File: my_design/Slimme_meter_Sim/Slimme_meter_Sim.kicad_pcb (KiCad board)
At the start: 2 copper layers, 29 parts, among them CN1 S2B-PH-SM4-TB, SW1 MSK12C02, U1 USBLC6-2SC6-ES, U2 BQ25185DLHR, U3 TPS61023DRLR

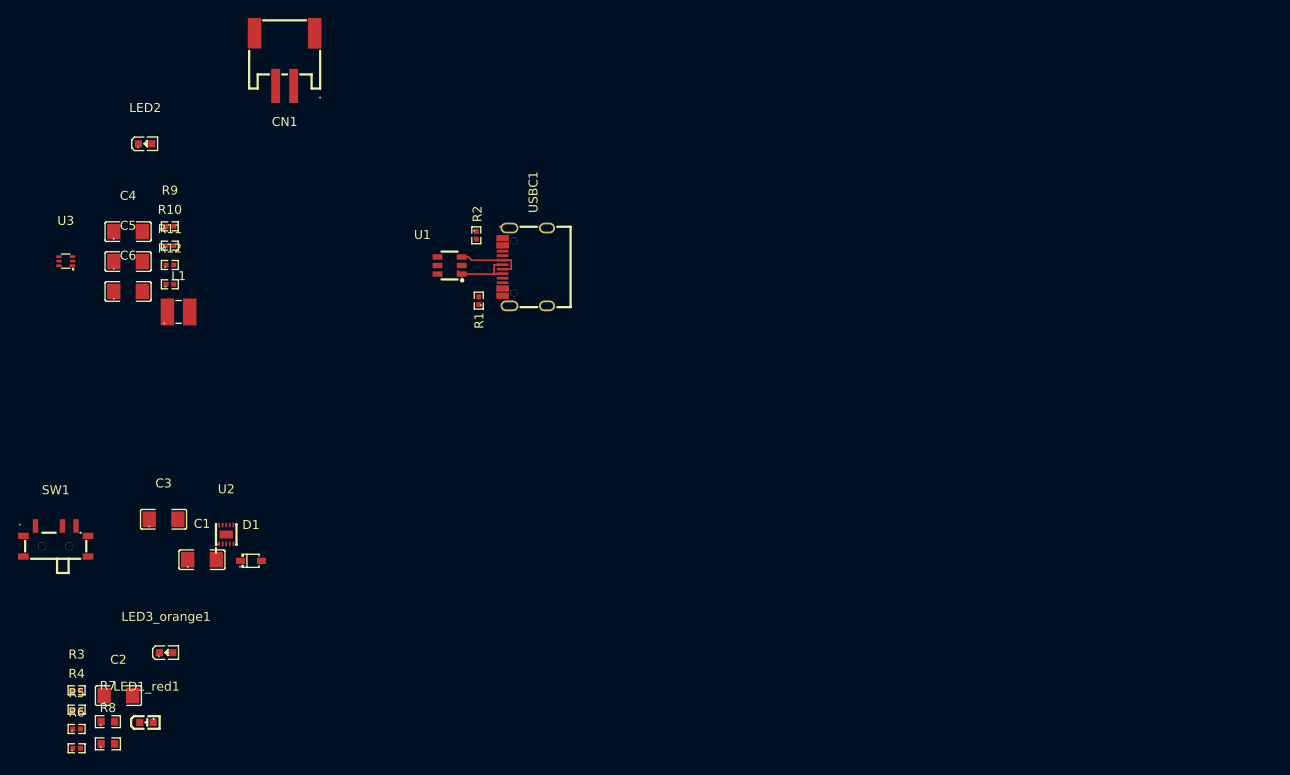
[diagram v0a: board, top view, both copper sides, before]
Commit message: Add sheet-2 power/MCU schematic progress and document P1 opto domains.
Captures TPS26625, SY8088 3V3, ESP32-C3, RJ12 placement, and README guidance that Request/Data optos keep UART on 3.3 V while pin 5 stays open-collector on the 5 V P1 side.

Co-authored-by: Cursor <cursoragent@cursor.com>
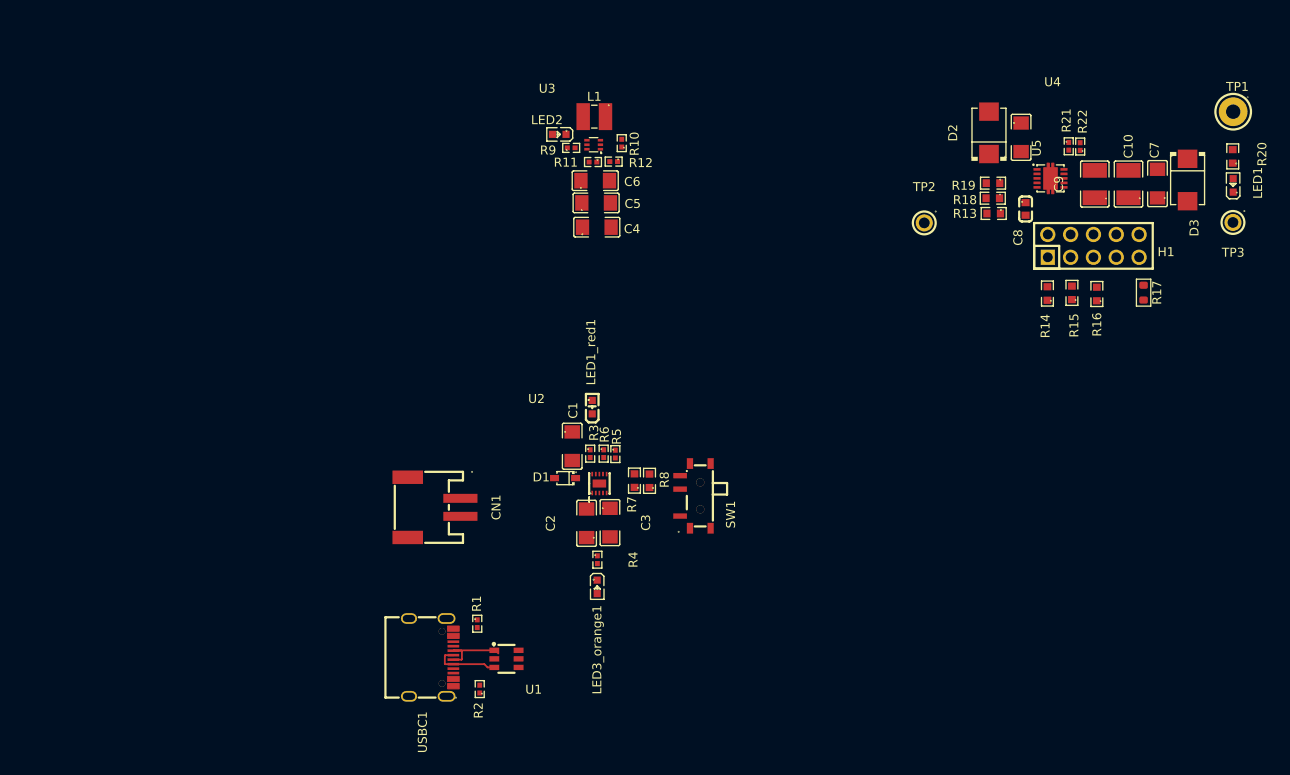
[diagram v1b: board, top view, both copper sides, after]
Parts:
- added C10: GRM32ER71J106KA12L_C437568, EasyEDA:C1210, F.Cu at (137.2, 56.1)
- added C7: C1206C225K3RACTU, EasyEDA:C1206, F.Cu at (140.4, 56.0)
- added C8: GRM188R71H223KA01D, EasyEDA:C0603, F.Cu at (125.7, 58.9)
- added C9: GRM32ER71J106KA12L_C437568, EasyEDA:C1210, F.Cu at (133.4, 56.1)
- added D2: SMBJ5.0A-13-F, EasyEDA:SMB_L4.6-W3.6-LS5.3-RD, F.Cu at (121.6, 50.4)
- added D3: SMBJ5.0A-13-F, EasyEDA:SMB_L4.6-W3.6-LS5.3-RD, F.Cu at (143.7, 55.6)
- added H1: DS1023-2*5SF11, EasyEDA:HDR-TH_10P-P2.54-V-F-R2-C5-S2.54, F.Cu at (133.2, 63.0)
- added LED1: 0603 Green 509-620mcd, EasyEDA:LED0603-RD, F.Cu at (148.8, 56.2)
- added R13: CR0603-FX-3012ELF, EasyEDA:R0603, F.Cu at (122.2, 59.4)
- added R14: CRCW06037K50FKEA, EasyEDA:R0603, F.Cu at (128.1, 68.3)
- added R15: RS-03K1332FT, EasyEDA:R0603, F.Cu at (130.9, 68.2)
- added R16: AR03FTC2672, EasyEDA:R0603, F.Cu at (133.6, 68.3)
- added R17: HRC0603F2673ENTN, PCM_Resistor_SMD_AKL:R_0603_1608Metric, F.Cu at (138.8, 68.2)
- added R18: CR0603-FX-3742ELF, EasyEDA:R0603, F.Cu at (122.0, 57.6)
- added R19: RS-03K1583FT, EasyEDA:R0603, F.Cu at (122.1, 56.0)
- added R20: AR03FTC2672, EasyEDA:R0603, F.Cu at (148.8, 53.0)
- added R21: 0402WGF1003TCE, EasyEDA:R0402, F.Cu at (130.5, 51.9)
- added R22: 0402WGF1003TCE, EasyEDA:R0402, F.Cu at (131.8, 51.9)
- added TP1: RH-5117, EasyEDA:TESTPOINT-TH_BD3.2-D1.6, F.Cu at (148.8, 48.0)
- added TP2: RH-5002, EasyEDA:TESTPOINT-TH_BD2.5-D1.2_RH-5002, F.Cu at (114.4, 60.4)
- added TP3: RH-5002, EasyEDA:TESTPOINT-TH_BD2.5-D1.2_RH-5002, F.Cu at (148.8, 60.4)
- added U4: TPS26625DRCR, EasyEDA:VSON-10_L3.0-W3.0-P0.50-TL-EP-1, F.Cu at (128.5, 55.4)
- added U5: C1206C105K3RACAUTO, EasyEDA:C1206, F.Cu at (125.2, 50.9)
- moved SW1 71.4 mm to (89.0, 90.8), turned to 90 degrees
- moved R5 67.3 mm to (80.0, 86.1), turned to -90 degrees
- moved R6 67.2 mm to (78.8, 86.1), turned to -90 degrees
- moved R8 67.0 mm to (83.8, 89.1), turned to 90 degrees
- moved R7 64.4 mm to (82.2, 89.1), turned to 90 degrees
- moved R3 62.9 mm to (77.2, 86.1), turned to -90 degrees
- moved LED1_red1 60.8 mm to (77.5, 80.9), turned to 90 degrees
- moved R4 60.3 mm to (78.0, 97.9), turned to -90 degrees
- moved U3 60.2 mm to (77.6, 51.7)
- moved C2 55.5 mm to (76.8, 93.8), turned to 90 degrees
- moved C6 53.4 mm to (77.8, 55.7)
- moved CN1 52.5 mm to (59.9, 92.0), turned to -90 degrees
- moved C5 52.5 mm to (77.9, 58.2)
- moved C4 52.2 mm to (78.0, 60.9)
- moved R10 51.6 mm to (80.8, 51.5), turned to 90 degrees
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
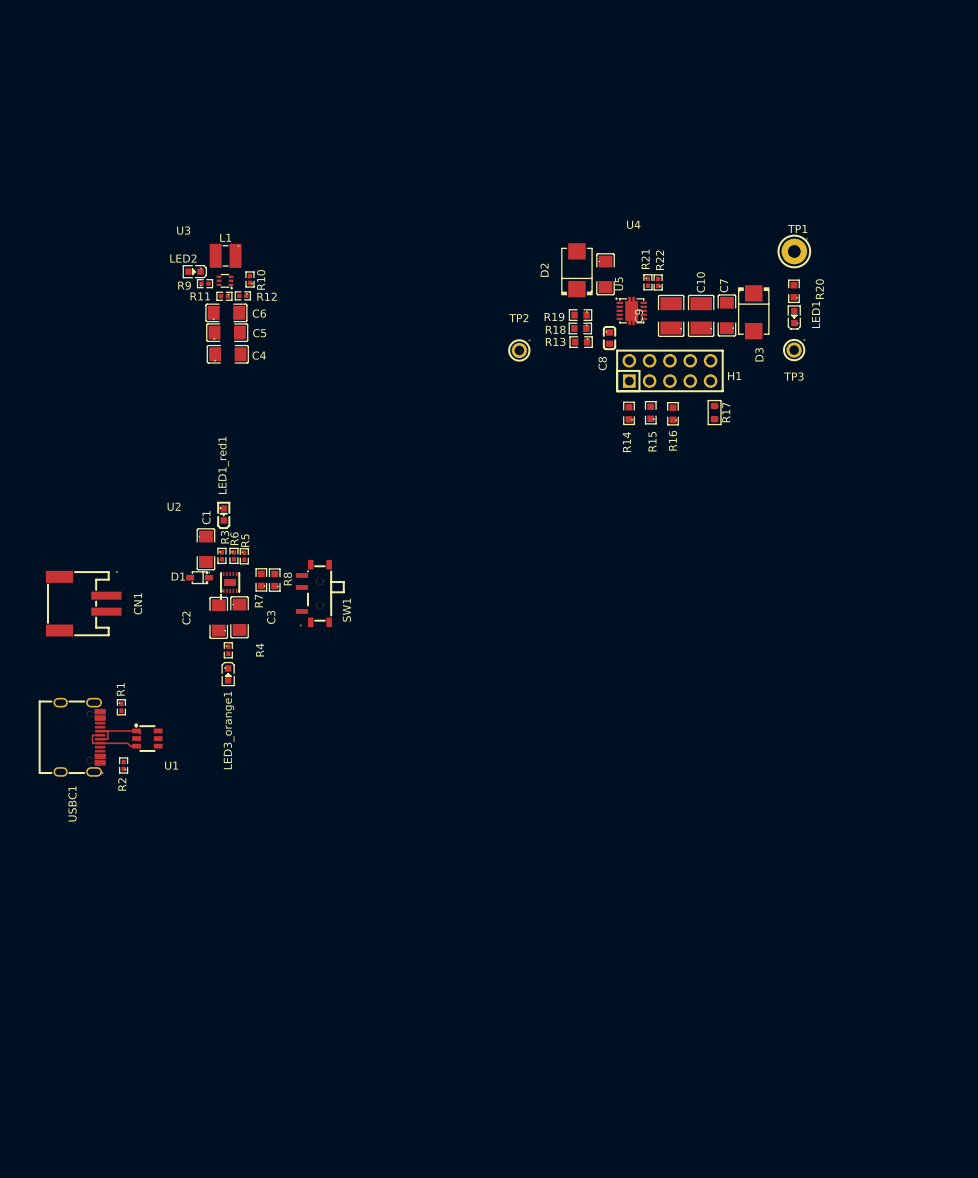
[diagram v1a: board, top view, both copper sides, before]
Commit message: Save KiCad schematic/PCB progress and park Pi next-step ideas.
Document assembly (stencil + hot air) and the dual-domain Pi brain option so the ESP32 path can be resumed cleanly tomorrow.

Co-authored-by: Cursor <cursoragent@cursor.com>
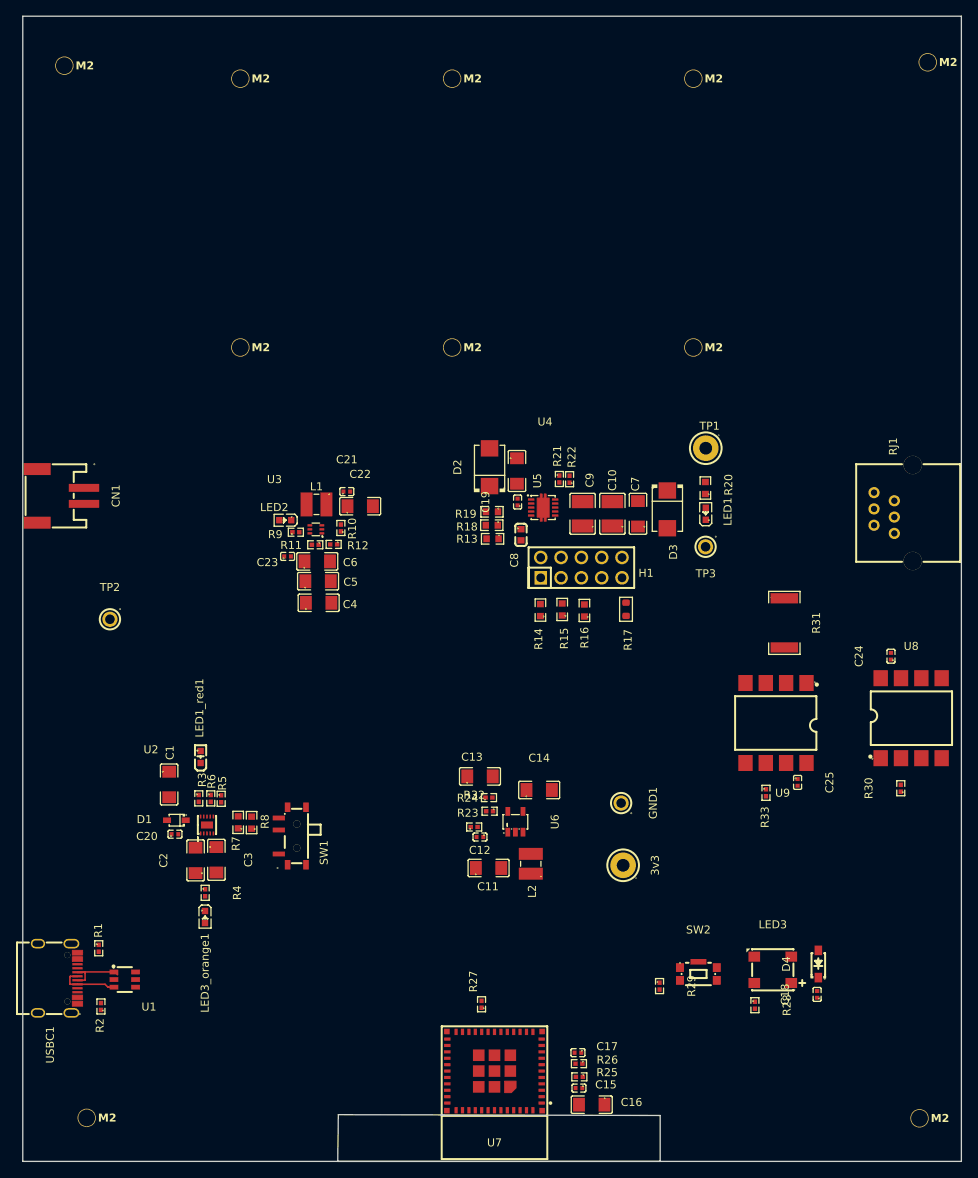
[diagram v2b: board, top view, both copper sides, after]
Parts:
- added 3v3: RH-5117, EasyEDA:TESTPOINT-TH_BD3.2-D1.6, F.Cu at (127.4, 124.8)
- added C11: FS31X226M160EPG, EasyEDA:C1206, F.Cu at (110.6, 125.1)
- added C12: CL05A105KA5NQNC, EasyEDA:C0402, F.Cu at (109.5, 121.2)
- added C13: FS31X226M160EPG, EasyEDA:C1206, F.Cu at (109.5, 113.6)
- added C14: FS31X226M160EPG, EasyEDA:C1206, F.Cu at (116.9, 115.3)
- added C15: CL05B104KO5NNNC, EasyEDA:C0402, F.Cu at (121.9, 152.6)
- added C16: FS31X226M160EPG, EasyEDA:C1206, F.Cu at (123.5, 154.7)
- added C17: CL05A105KA5NQNC, EasyEDA:C0402, F.Cu at (121.8, 148.2)
- added C18: CL05B104KO5NNNC, EasyEDA:C0402, F.Cu at (151.6, 140.9)
- added C19: CL05B104KO5NNNC, EasyEDA:C0402, F.Cu at (114.2, 79.3)
- added C20: CL05B104KO5NNNC, EasyEDA:C0402, F.Cu at (71.4, 120.9)
- added C21: CL05B104KO5NNNC, EasyEDA:C0402, F.Cu at (92.9, 78.0)
- added C22: FS31X226M160EPG, EasyEDA:C1206, F.Cu at (94.5, 79.9)
- added C23: CL05B104KO5NNNC, EasyEDA:C0402, F.Cu at (85.5, 86.1)
- added C24: CL05B104KO5NNNC, EasyEDA:C0402, F.Cu at (160.9, 98.6)
- added C25: CL05B104KO5NNNC, EasyEDA:C0402, F.Cu at (149.2, 114.4)
- added D4: B5819W_C8598, EasyEDA:SOD-123_L2.7-W1.6-LS3.7-RD-1, F.Cu at (151.8, 137.1)
- added GND1: RH-5002, EasyEDA:TESTPOINT-TH_BD2.5-D1.2_RH-5002, F.Cu at (127.2, 117.0)
- added H10: ~, PCM_fab:MountingHole_M2, F.Cu at (136.2, 26.4)
- added H11: ~, PCM_fab:MountingHole_M2, F.Cu at (136.2, 60.0)
- added H2: ~, PCM_fab:MountingHole_M2, F.Cu at (164.4, 156.4)
- added H3: ~, PCM_fab:MountingHole_M2, F.Cu at (165.5, 24.4)
- added H4: ~, PCM_fab:MountingHole_M2, F.Cu at (57.5, 24.8)
- added H5: ~, PCM_fab:MountingHole_M2, F.Cu at (60.4, 156.3)
- added H6: ~, PCM_fab:MountingHole_M2, F.Cu at (79.5, 26.4)
- added H7: ~, PCM_fab:MountingHole_M2, F.Cu at (79.5, 60.0)
- added H8: ~, PCM_fab:MountingHole_M2, F.Cu at (106.0, 26.4)
- added H9: ~, PCM_fab:MountingHole_M2, F.Cu at (106.0, 60.0)
- added L2: MDTA32251B-2R2M, EasyEDA:IND-SMD_L3.2-W2.5-BRL3225T100M, F.Cu at (115.9, 124.6)
- added LED3: DY-S505016/RGBC/6812F-NL-1T, EasyEDA:LED-SMD_4P-L5.0-W5.0-BR, F.Cu at (146.1, 137.8)
- added R23: RT0402FRE07309RL, EasyEDA:R0402, F.Cu at (110.7, 118.0)
- added R24: SCR0402F68R1, EasyEDA:R0402, F.Cu at (110.6, 116.3)
- added R25: AR02BTC1002, EasyEDA:R0402, F.Cu at (121.9, 151.2)
- added R26: AR02BTC1002, EasyEDA:R0402, F.Cu at (121.9, 149.6)
- added R27: AR02BTC1002, EasyEDA:R0402, F.Cu at (109.7, 142.1)
- added R28: 0402WGF3300TCE, EasyEDA:R0402, F.Cu at (143.9, 142.2)
- added R29: AR02BTC1002, EasyEDA:R0402, F.Cu at (131.9, 139.8)
- added R30: MCS04020C2200FE000, EasyEDA:R0402, F.Cu at (162.1, 115.1)
- added R31: 25121WJ0331T4E, EasyEDA:R2512, F.Cu at (147.6, 94.5)
- added R32: AR02BTC1002, EasyEDA:R0402, F.Cu at (108.8, 120.0)
- added R33: AR02BTC1002, EasyEDA:R0402, F.Cu at (145.3, 115.7)
- added RJ1: KH-PCB-6P6C, EasyEDA:RJ45-TH_KH-PCB-6P6C, F.Cu at (160.0, 80.7)
- added SW2: KMR231GLFS, EasyEDA:KEY-SMD_KMR2XXGXXX, F.Cu at (136.8, 138.0)
- added U6: SY8088AAC, EasyEDA:SOT-23-5_L3.0-W1.7-P0.95-LS2.8-BR, F.Cu at (113.9, 119.3)
- added U7: ESP32-C3-MINI-1-H4X, EasyEDA:WIFIM-SMD_ESP32-C3-MINI-1, F.Cu at (111.3, 150.5)
- added U8: 6N137S_C20612601, EasyEDA:SOP-8_L9.7-W6.5-P2.54-LS10.3-BL, F.Cu at (163.4, 106.4)
- added U9: 6N137S_C20612601, EasyEDA:SOP-8_L9.7-W6.5-P2.54-LS10.3-BL, F.Cu at (146.5, 107.0)
- moved TP2 61.2 mm to (63.2, 94.0)
- moved C4 33.1 mm to (89.3, 91.9)
- moved C5 33.1 mm to (89.3, 89.2)
- moved C6 33.1 mm to (89.2, 86.8)
- moved L1 33.1 mm to (89.1, 79.6)
- moved LED2 33.1 mm to (85.2, 81.6)
- moved R10 33.1 mm to (92.1, 82.6)
- moved R11 33.1 mm to (88.9, 84.7)
- moved R12 33.1 mm to (91.2, 84.6)
- moved R9 33.1 mm to (86.5, 83.1)
- moved U3 33.1 mm to (89.0, 82.8)
- moved R8 30.5 mm to (81.0, 119.4)
- moved LED3_orange1 30.5 mm to (75.1, 131.2)
- moved SW1 30.5 mm to (86.1, 121.1)
- moved U2 30.5 mm to (75.4, 119.7)
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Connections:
- net Net-(D3-C) renamed RJ12_5V
- R19 pad 2: Net-(U4-IN) -> +5V
- R21 pad 1: Net-(U4-IN) -> +5V
- R22 pad 2: Net-(U4-IN) -> +5V
- U4 pad 1: Net-(U4-IN) -> +5V
- U4 pad 11: unconnected-(U4-EP-Pad11) -> GND1
- U5 pad 2: Net-(U4-IN) -> +5V
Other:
- board outline added: 117.3 x 143.1 mm
